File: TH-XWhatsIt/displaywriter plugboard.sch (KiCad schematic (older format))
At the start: 4 parts, among them J10 DISPLAYWRITER PLUGBOARD CONNE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, J11 DISPLAYWRITER PLUGBOARD ROWS, J9 DISPLAYWRITER PLUGBOARD COLUM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

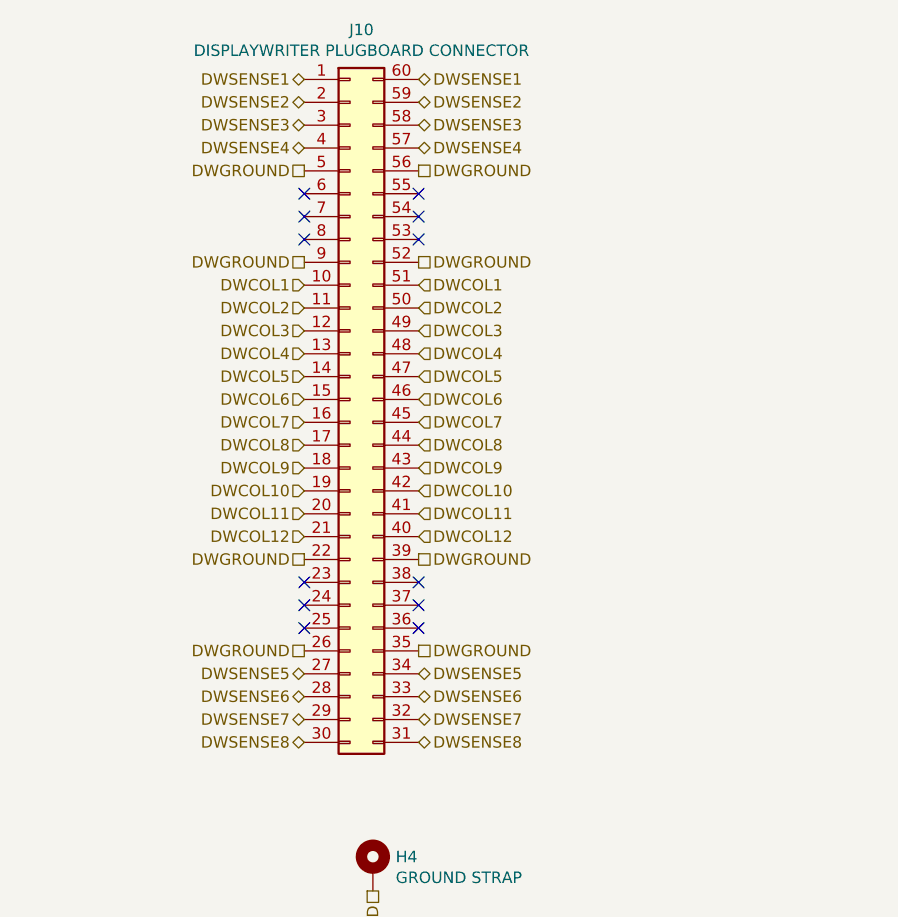
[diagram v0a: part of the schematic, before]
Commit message: displaywriter plugboard: Make sure we don't interfere with mounting plate. Add support for different vertical pin pitch connectors. Add support for original connector with mounting slot. Position of mounting slot is experimental, measurements were made by counting pixels on images.
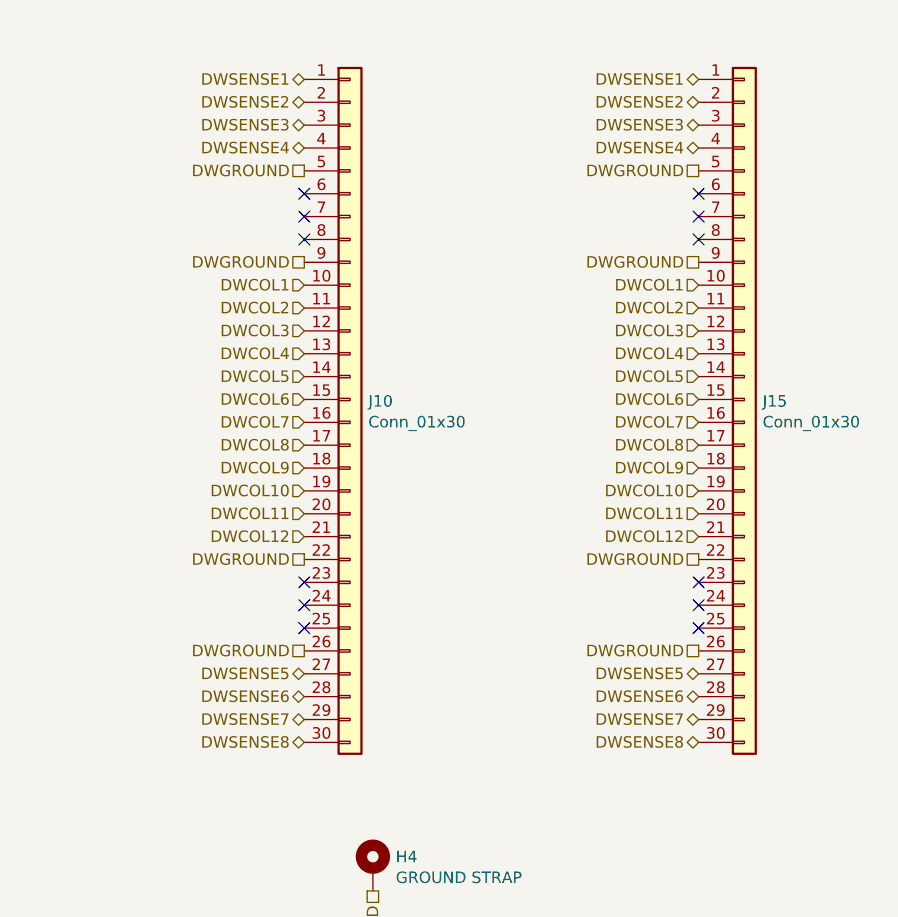
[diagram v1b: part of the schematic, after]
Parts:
- removed J10: DISPLAYWRITER PLUGBOARD CONNECTOR, TH-XWhatsIt:DIP-60_155_ELL, symbol Connector_Generic:Conn_02x30_Counter_Clockwise
- added J10: Conn_01x30, TH-XWhatsIt:displaywriter-connector_v3, symbol Connector_Generic:Conn_01x30
- added J15: Conn_01x30, TH-XWhatsIt:Model_F_3.96mm_pitch_footprint, symbol Connector_Generic:Conn_01x30
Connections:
- net DWCOL1: now also J10.10 (Pin_10), J15.10 (Pin_10)
- net DWCOL10: now also J10.19 (Pin_19), J15.19 (Pin_19)
- net DWCOL11: now also J10.20 (Pin_20), J15.20 (Pin_20)
- net DWCOL12: now also J10.21 (Pin_21), J15.21 (Pin_21)
- net DWCOL2: now also J10.11 (Pin_11), J15.11 (Pin_11)
- net DWCOL3: now also J10.12 (Pin_12), J15.12 (Pin_12)
- net DWCOL4: now also J10.13 (Pin_13), J15.13 (Pin_13)
- net DWCOL5: now also J10.14 (Pin_14), J15.14 (Pin_14)
- net DWCOL6: now also J10.15 (Pin_15), J15.15 (Pin_15)
- net DWCOL7: now also J10.16 (Pin_16), J15.16 (Pin_16)
- net DWCOL8: now also J10.17 (Pin_17), J15.17 (Pin_17)
- net DWCOL9: now also J10.18 (Pin_18), J15.18 (Pin_18)
- net DWGROUND: now also J10.22 (Pin_22), J10.26 (Pin_26), J10.5 (Pin_5), J10.9 (Pin_9), J15.22 (Pin_22), J15.26 (Pin_26), J15.5 (Pin_5), J15.9 (Pin_9)
- net DWSENSE1: now also J10.1 (Pin_1), J15.1 (Pin_1)
- net DWSENSE2: now also J10.2 (Pin_2), J15.2 (Pin_2)
- net DWSENSE3: now also J10.3 (Pin_3), J15.3 (Pin_3)
- net DWSENSE4: now also J10.4 (Pin_4), J15.4 (Pin_4)
- net DWSENSE5: now also J10.27 (Pin_27), J15.27 (Pin_27)
- net DWSENSE6: now also J10.28 (Pin_28), J15.28 (Pin_28)
- net DWSENSE7: now also J10.29 (Pin_29), J15.29 (Pin_29)
- net DWSENSE8: now also J10.30 (Pin_30), J15.30 (Pin_30)
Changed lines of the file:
@@
 Copyright Rainy Day Plans.\nThis documentation describes Open Hardware and is licensed under the\nCERN OHL v. 1.2.\nYou may redistribute and modify this documentation under the terms of the\nCERN OHL v.1.2. (http://ohwr.org/cernohl). This documentation is distributed\nWITHOUT ANY EXPRESS OR IMPLIED WARRANTY, INCLUDING OF\nMERCHANTABILITY, SATISFACTORY QUALITY AND FITNESS FOR A\nPARTICULAR PURPOSE. Please see the CERN OHL v.1.2 for applicable\nconditions
-$Comp
-L Connector_Generic:Conn_02x30_Counter_Clockwise J10
-U 1 1 5E4284EA
-P 6675 2775
-F 0 "J10" H 6725 4392 50  0000 C CNN
-F 1 "DISPLAYWRITER PLUGBOARD CONNECTOR" H 6725 4301 50  0000 C CNN
-F 2 "TH-XWhatsIt:DIP-60_155_ELL" H 6675 2775 50  0001 C CNN
-F 3 "~" H 6675 2775 50  0001 C CNN
-	1    6675 2775
-	1    0    0    -1
-$EndComp
-NoConn ~ 6975 3575
-NoConn ~ 6975 3675
-NoConn ~ 6975 3775
-NoConn ~ 6975 1875
-NoConn ~ 6975 1975
-NoConn ~ 6975 2075
-Text HLabel 6975 1375 2    50   BiDi ~ 0
-DWSENSE1
-Text HLabel 6975 1475 2    50   BiDi ~ 0
-DWSENSE2
-Text HLabel 6975 1575 2    50   BiDi ~ 0
-DWSENSE3
-Text HLabel 6975 1675 2    50   BiDi ~ 0
-DWSENSE4
-Text HLabel 6975 3975 2    50   BiDi ~ 0
-DWSENSE5
-Text HLabel 6975 4075 2    50   BiDi ~ 0
-DWSENSE6
-Text HLabel 6975 4175 2    50   BiDi ~ 0
-DWSENSE7
-Text HLabel 6975 4275 2    50   BiDi ~ 0
-DWSENSE8
-Text HLabel 6975 2275 2    50   Input ~ 0
-DWCOL1
-Text HLabel 6975 2375 2    50   Input ~ 0
-DWCOL2
-Text HLabel 6975 2475 2    50   Input ~ 0
-DWCOL3
-Text HLabel 6975 2575 2    50   Input ~ 0
-DWCOL4
-Text HLabel 6975 2675 2    50   Input ~ 0
-DWCOL5
-Text HLabel 6975 2775 2    50   Input ~ 0
-DWCOL6
-Text HLabel 6975 2875 2    50   Input ~ 0
-DWCOL7
-Text HLabel 6975 2975 2    50   Input ~ 0
-DWCOL8
-Text HLabel 6975 3075 2    50   Input ~ 0
-DWCOL9
-Text HLabel 6975 3175 2    50   Input ~ 0
-DWCOL10
-Text HLabel 6975 3275 2    50   Input ~ 0
-DWCOL11
-Text HLabel 6975 3375 2    50   Input ~ 0
-DWCOL12
-Text HLabel 6975 1775 2    50   UnSpc ~ 0
-DWGROUND
-Text HLabel 6975 2175 2    50   UnSpc ~ 0
-DWGROUND
-Text HLabel 6975 3475 2    50   UnSpc ~ 0
-DWGROUND
-Text HLabel 6975 3875 2    50   UnSpc ~ 0
-DWGROUND
 $Comp
 L Mechanical:MountingHole_Pad H4
@@
 Text HLabel 6775 4925 3    50   UnSpc ~ 0
 DWGROUND
+$Comp
+L Connector_Generic:Conn_01x30 J10
+U 1 1 5F4814DA
+P 6675 2775
+F 0 "J10" H 6755 2767 50  0000 L CNN
+F 1 "Conn_01x30" H 6755 2676 50  0000 L CNN
+F 2 "TH-XWhatsIt:displaywriter-connector_v3" H 6675 2775 50  0001 C CNN
+F 3 "~" H 6675 2775 50  0001 C CNN
+	1    6675 2775
+	1    0    0    -1
+$EndComp
+$Comp
+L Connector_Generic:Conn_01x30 J15
+U 1 1 5F49C915
+P 8400 2775
+F 0 "J15" H 8480 2767 50  0000 L CNN
+F 1 "Conn_01x30" H 8480 2676 50  0000 L CNN
+F 2 "TH-XWhatsIt:Model_F_3.96mm_pitch_footprint" H 8400 2775 50  0001 C CNN
+F 3 "~" H 8400 2775 50  0001 C CNN
+	1    8400 2775
+	1    0    0    -1
+$EndComp
+Text HLabel 8200 1375 0    50   BiDi ~ 0
+DWSENSE1
+Text HLabel 8200 1475 0    50   BiDi ~ 0
+DWSENSE2
+Text HLabel 8200 1575 0    50   BiDi ~ 0
+DWSENSE3
+Text HLabel 8200 1675 0    50   BiDi ~ 0
+DWSENSE4
+Text HLabel 8200 1775 0    50   UnSpc ~ 0
+DWGROUND
+Text HLabel 8200 2175 0    50   UnSpc ~ 0
+DWGROUND
+Text HLabel 8200 2275 0    50   Input ~ 0
+DWCOL1
+Text HLabel 8200 2375 0    50   Input ~ 0
+DWCOL2
+Text HLabel 8200 2475 0    50   Input ~ 0
+DWCOL3
+Text HLabel 8200 2575 0    50   Input ~ 0
+DWCOL4
+Text HLabel 8200 2675 0    50   Input ~ 0
+DWCOL5
+Text HLabel 8200 2775 0    50   Input ~ 0
+DWCOL6
+Text HLabel 8200 2875 0    50   Input ~ 0
+DWCOL7
+Text HLabel 8200 2975 0    50   Input ~ 0
+DWCOL8
+Text HLabel 8200 3075 0    50   Input ~ 0
+DWCOL9
+Text HLabel 8200 3175 0    50   Input ~ 0
+DWCOL10
+Text HLabel 8200 3275 0    50   Input ~ 0
+DWCOL11
+Text HLabel 8200 3375 0    50   Input ~ 0
+DWCOL12
+Text HLabel 8200 3475 0    50   UnSpc ~ 0
+DWGROUND
+Text HLabel 8200 3875 0    50   UnSpc ~ 0
+DWGROUND
+Text HLabel 8200 3975 0    50   BiDi ~ 0
+DWSENSE5
+Text HLabel 8200 4075 0    50   BiDi ~ 0
+DWSENSE6
+Text HLabel 8200 4175 0    50   BiDi ~ 0
+DWSENSE7
+Text HLabel 8200 4275 0    50   BiDi ~ 0
+DWSENSE8
+NoConn ~ 8200 3775
+NoConn ~ 8200 3675
+NoConn ~ 8200 3575
+NoConn ~ 8200 1875
+NoConn ~ 8200 1975
+NoConn ~ 8200 2075
 $EndSCHEMATC

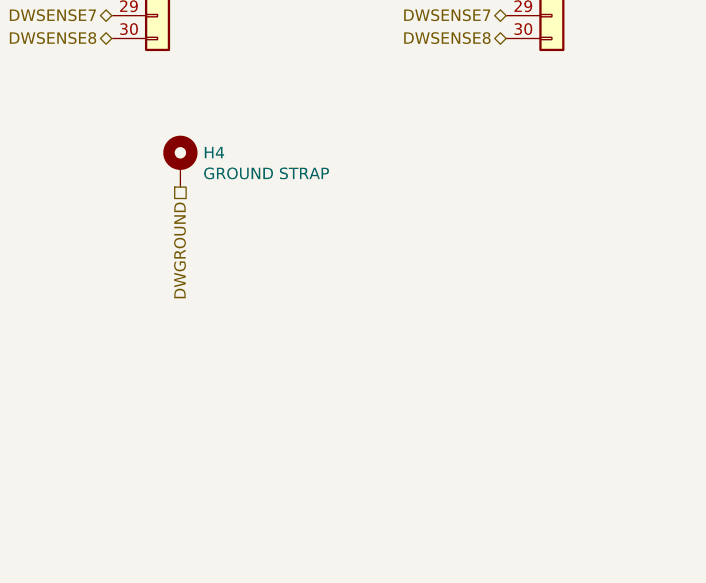
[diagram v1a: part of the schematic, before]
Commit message: Various changes to revision 0.1.1
General:
    Made mounting hole bigger (M3). And moved it a little bit so it doesn't interfere with some components.
    Star ground turned into single ground.
    Ground fills added everywhere.
    Many stitching vias added everywhere.
    Added JLCJLCJLCJLC magic string under pro micro. When ordering from JLCPCB, you can select for Order Number: "Specify Location"
    Bumped version number to 0.1.1
    Added silkscreen to mark rows/columns everywhere.
    Added optional holes for soldering grounding wires everywhere.
Controller:
    Added silkscreen to ease debugging, by marking various important nets.
    Rearranged some traces to maintain better separation between traces, and better ground reference.
Model F plugboard:
    Modified 3.96mm pitch holes, to hole sizes and pad sizes that match original xwhatsit model F controller
    Moved 3.96mm pitch holes closer to the edge, so it doesn't interfere with case in F AT cases.
    Added mounting holes
    Added holes to support 3178 keyboards.
Displaywriter:
    Addes support for more connector types. (The displaywriter daughterboard is now taller)
Beamspring:
    Bugfix to a mistake that only affected people that ran update footprints from library.
Beamship daughterboard:
    Added support for more connectors. Added breakoff-able mounting hole.
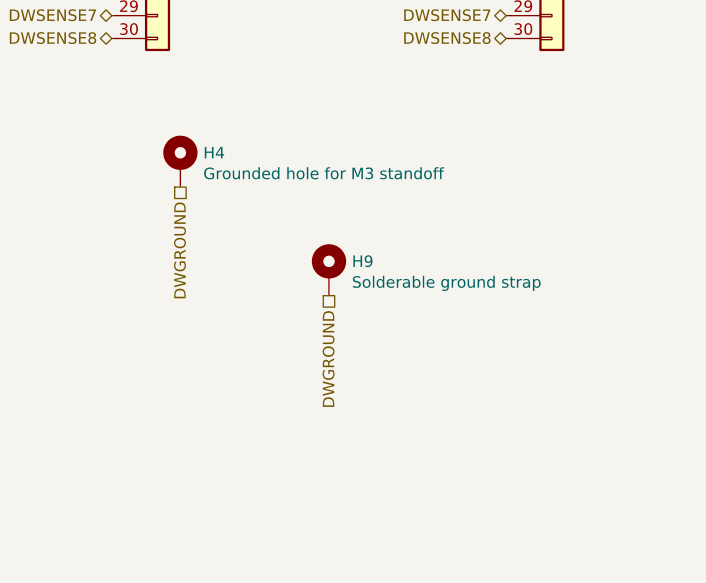
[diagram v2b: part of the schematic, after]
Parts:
- added H9: Solderable ground strap, TH-XWhatsIt:ChassisGnd, symbol Mechanical:MountingHole_Pad
- H4: value GROUND STRAP -> Grounded hole for M3 standoff; footprint MountingHole:MountingHole_2.2mm_M2_Pad_Via -> MountingHole:MountingHole_3.2mm_M3_Pad_Via
- J15: footprint TH-XWhatsIt:Model_F_3.96mm_pitch_footprint -> TH-XWhatsIt:Displaywriter_with_mountinghole_footprint
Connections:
- net DWGROUND: now also H9.1
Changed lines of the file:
@@
 P 6775 4825
 F 0 "H4" H 6875 4874 50  0000 L CNN
-F 1 "GROUND STRAP" H 6875 4783 50  0000 L CNN
-F 2 "MountingHole:MountingHole_2.2mm_M2_Pad_Via" H 6775 4825 50  0001 C CNN
+F 1 "Grounded hole for M3 standoff" H 6875 4783 50  0000 L CNN
+F 2 "MountingHole:MountingHole_3.2mm_M3_Pad_Via" H 6775 4825 50  0001 C CNN
 F 3 "~" H 6775 4825 50  0001 C CNN
 	1    6775 4825
@@
 F 0 "J15" H 8480 2767 50  0000 L CNN
 F 1 "Conn_01x30" H 8480 2676 50  0000 L CNN
-F 2 "TH-XWhatsIt:Model_F_3.96mm_pitch_footprint" H 8400 2775 50  0001 C CNN
+F 2 "TH-XWhatsIt:Displaywriter_with_mountinghole_footprint" H 8400 2775 50  0001 C CNN
 F 3 "~" H 8400 2775 50  0001 C CNN
 	1    8400 2775
@@
 NoConn ~ 8200 1975
 NoConn ~ 8200 2075
+$Comp
+L Mechanical:MountingHole_Pad H9
+U 1 1 5FBD3723
+P 7425 5300
+F 0 "H9" H 7525 5349 50  0000 L CNN
+F 1 "Solderable ground strap" H 7525 5258 50  0000 L CNN
+F 2 "TH-XWhatsIt:ChassisGnd" H 7425 5300 50  0001 C CNN
+F 3 "~" H 7425 5300 50  0001 C CNN
+	1    7425 5300
+	1    0    0    -1
+$EndComp
+Text HLabel 7425 5400 3    50   UnSpc ~ 0
+DWGROUND
 $EndSCHEMATC
